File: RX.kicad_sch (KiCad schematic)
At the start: 1 part, among them U3 AD8285WBCPZ

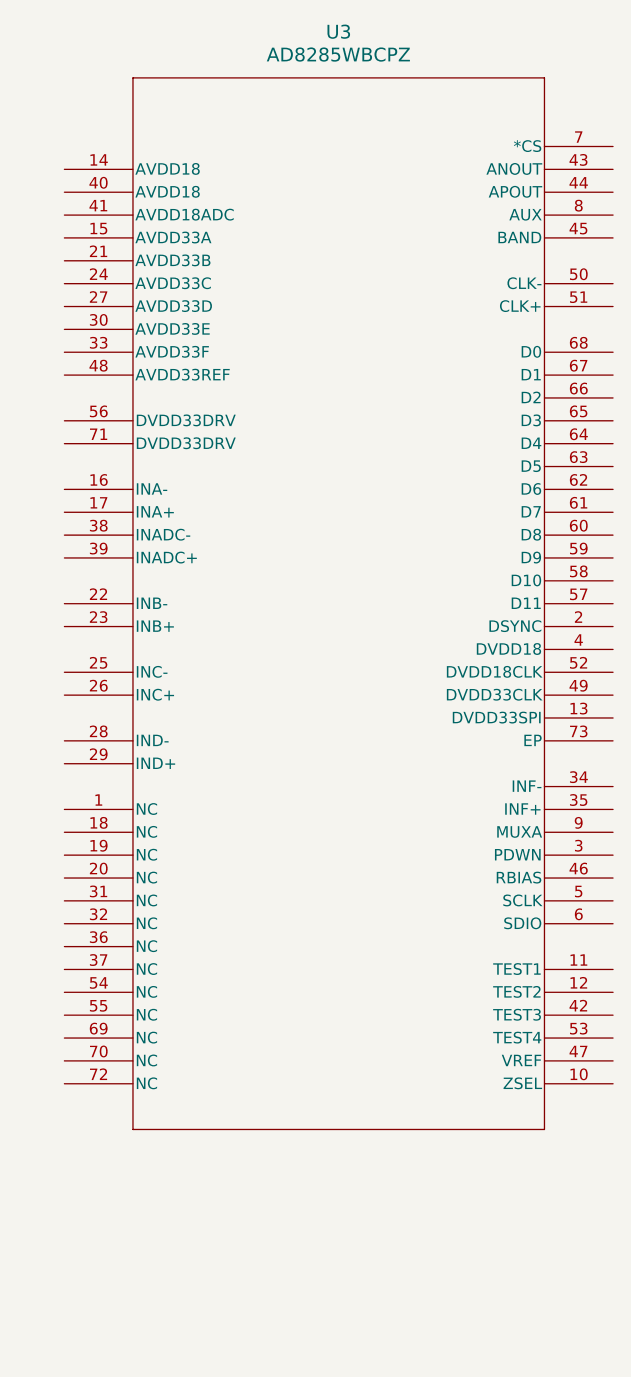
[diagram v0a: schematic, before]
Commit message: finished SOM 5V power, migrated altium stuff, finished pin study, added USB PHY (revise HS capability)
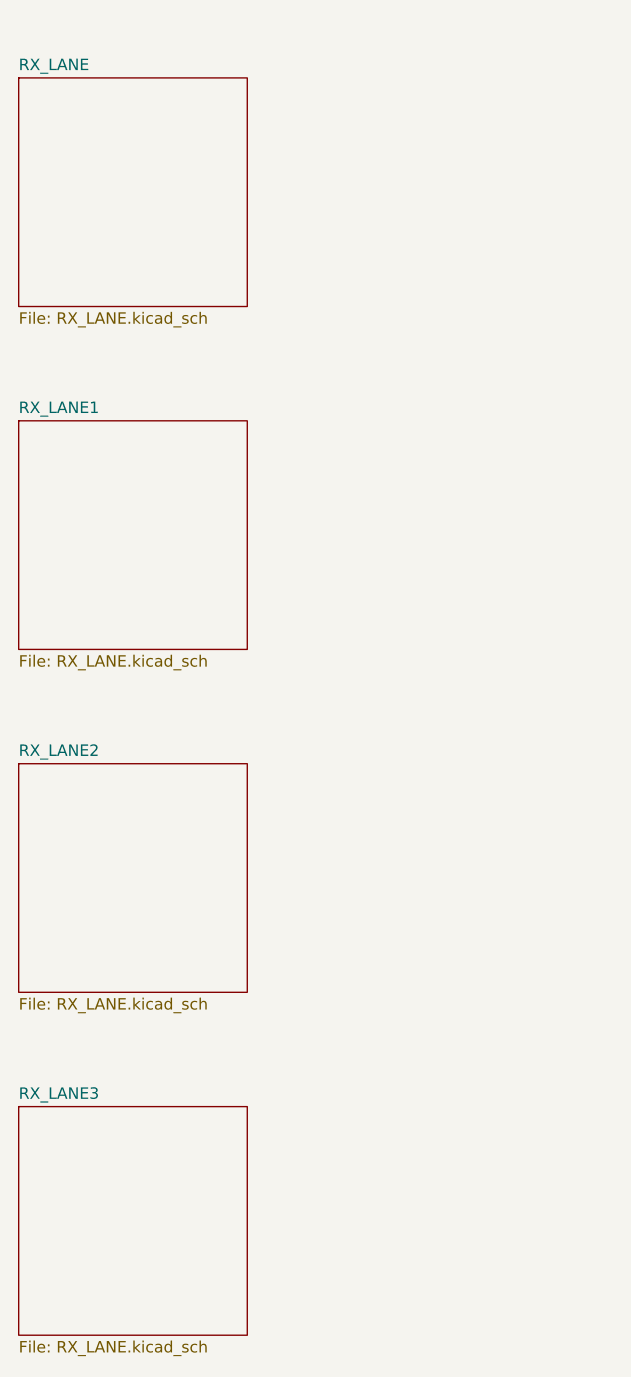
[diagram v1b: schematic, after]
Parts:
- removed U3: AD8285WBCPZ, CP_72_5_ADI, symbol AD8285WBCPZ:AD8285WBCPZ
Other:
- added sheet RX_LANE (RX_LANE.kicad_sch)
- added sheet RX_LANE1 (RX_LANE.kicad_sch)
- added sheet RX_LANE2 (RX_LANE.kicad_sch)
- added sheet RX_LANE3 (RX_LANE.kicad_sch)

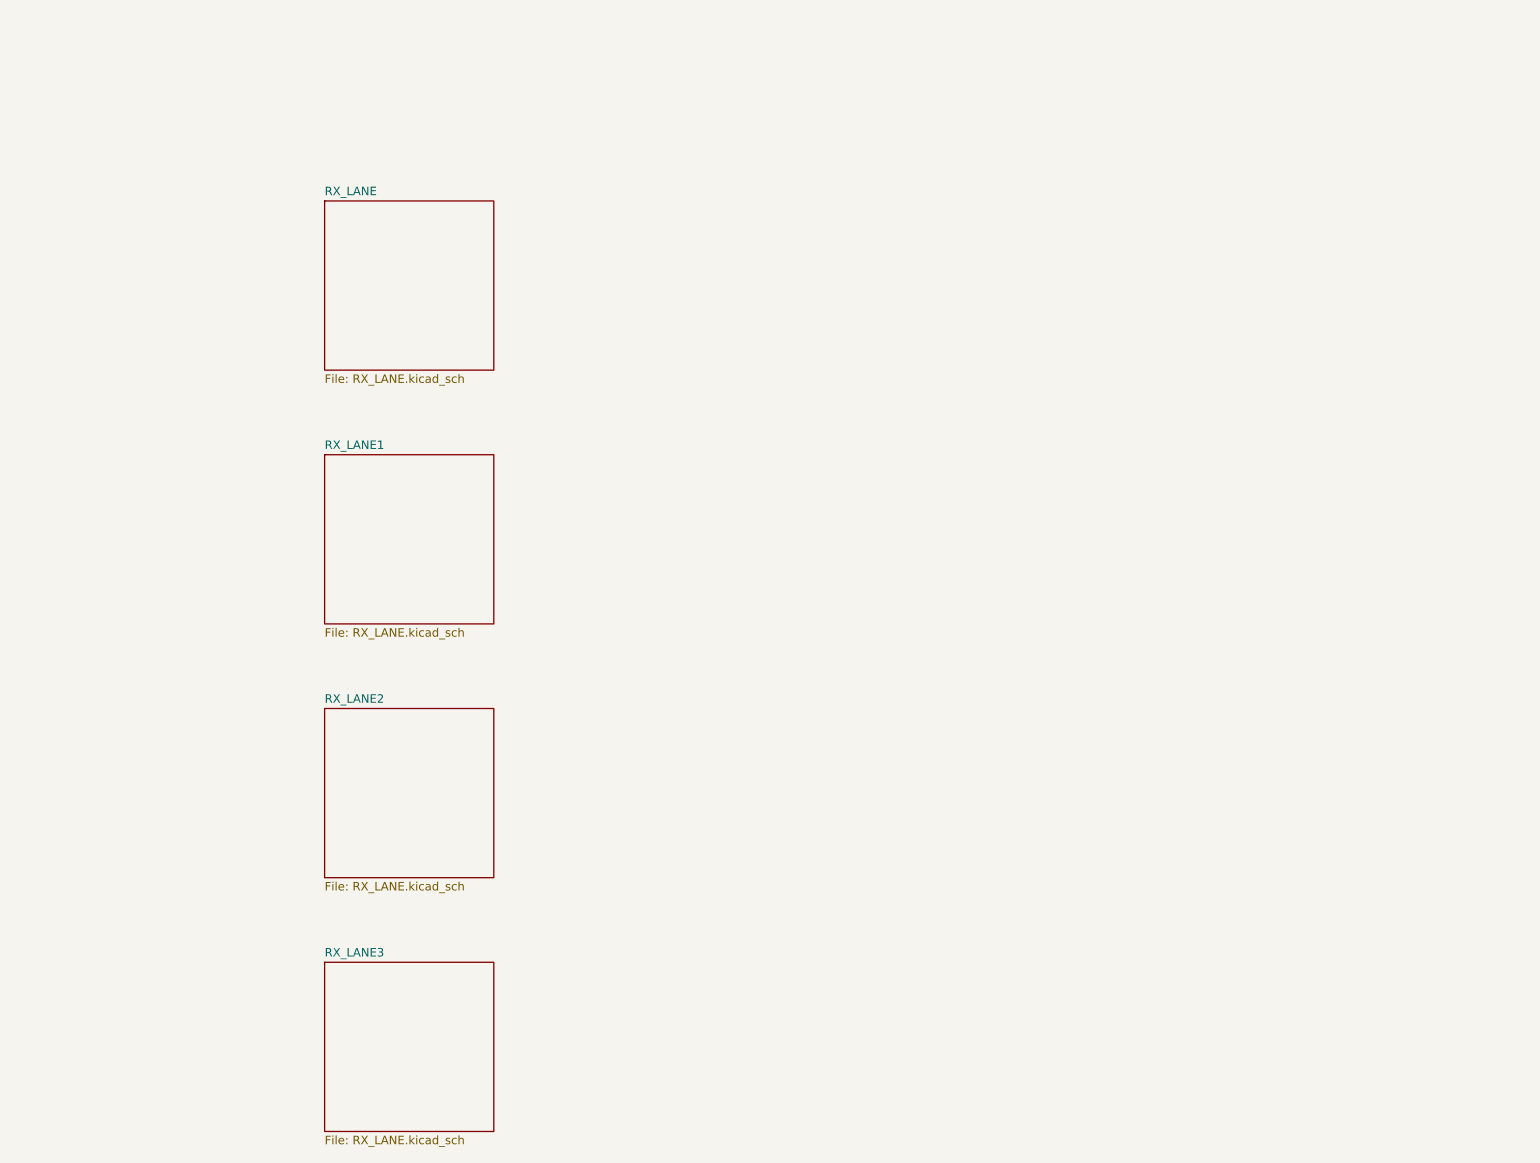
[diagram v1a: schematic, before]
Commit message: added ADC clock fanout, added 3A buck
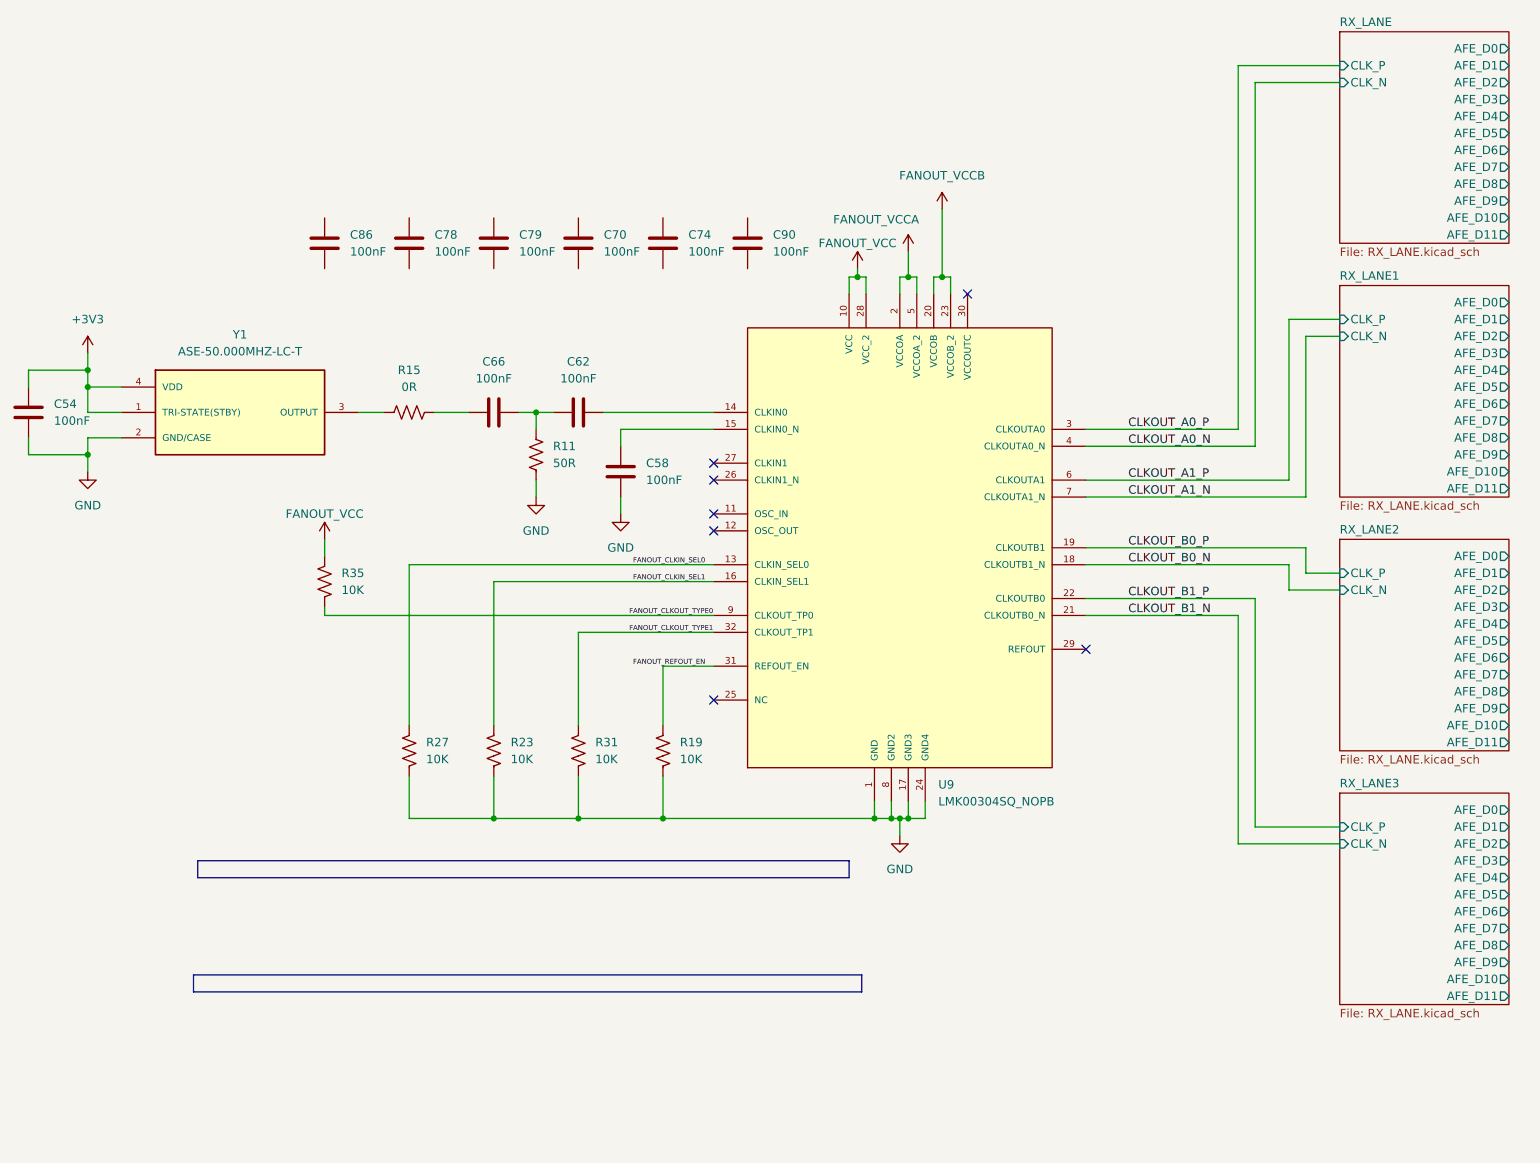
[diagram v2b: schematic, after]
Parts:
- added C54, C58, C62, C66, C70, C74, C78, C79, C86, C90: 100nF, symbol Device:C
- added R11: 50R, symbol Device:R_US
- added R15: 0R, symbol Device:R_US
- added R19, R23, R27, R31, R35: 10K, symbol Device:R_US
- added U9: LMK00304SQ_NOPB, LMK00304SQ_NOPB:WQFN-32, symbol LMK00304SQ_NOPB:LMK00304SQ_NOPB
- added Y1: ASE-50.000MHZ-LC-T, ASE-50.000MHZ-LC-T:XTAL_ASE-50.000MHZ-LC-T, symbol ASE-50.000MHZ-LC-T:ASE-50.000MHZ-LC-T
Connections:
- new net: R15.2, Y1.3 (OUTPUT)
- new net: C62.2, C66.1, R11.2
- new net: C66.2, R15.1
- new net: C62.1, U9.14 (CLKIN0)
- new net: C58.2, U9.15 (CLKIN0_N)
- new net +3V3: C54.2, Y1.1 (TRI-STATE(STBY)), Y1.4 (VDD)
- new net CLKOUT_A0_N: U9.4 (CLKOUTA0_N)
- new net CLKOUT_A0_P: U9.3 (CLKOUTA0)
- new net CLKOUT_A1_N: U9.7 (CLKOUTA1_N)
- new net CLKOUT_A1_P: U9.6 (CLKOUTA1)
- new net CLKOUT_B0_N: U9.18 (CLKOUTB1_N)
- new net CLKOUT_B0_P: U9.19 (CLKOUTB1)
- new net CLKOUT_B1_N: U9.21 (CLKOUTB0_N)
- new net CLKOUT_B1_P: U9.22 (CLKOUTB0)
- new net FANOUT_CLKIN_SEL0: R27.1, U9.13 (CLKIN_SEL0)
- new net FANOUT_CLKIN_SEL1: R23.1, U9.16 (CLKIN_SEL1)
- new net FANOUT_CLKOUT_TYPE0: R35.2, U9.9 (CLKOUT_TP0)
- new net FANOUT_CLKOUT_TYPE1: R31.1, U9.32 (CLKOUT_TP1)
- new net FANOUT_REFOUT_EN: R19.1, U9.31 (REFOUT_EN)
- new net FANOUT_VCC: R35.1, U9.10 (VCC), U9.28 (VCC_2)
- new net FANOUT_VCCA: U9.2 (VCCOA), U9.5 (VCCOA_2)
- new net FANOUT_VCCB: U9.20 (VCCOB), U9.23 (VCCOB_2)
- new net GND: C54.1, C58.1, R11.1, R19.2, R23.2, R27.2, R31.2, U9.1 (GND), U9.17 (GND3), U9.24 (GND4), U9.8 (GND2), Y1.2 (GND/CASE)
- no-connect marks 0 -> 7
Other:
- sheet RX_LANE ports: added AFE_D0, AFE_D1, AFE_D10, AFE_D11, AFE_D2, AFE_D3, AFE_D4, AFE_D5, AFE_D6, AFE_D7, AFE_D8, AFE_D9, CLK_N, CLK_P; removed none
- sheet RX_LANE1 ports: added AFE_D0, AFE_D1, AFE_D10, AFE_D11, AFE_D2, AFE_D3, AFE_D4, AFE_D5, AFE_D6, AFE_D7, AFE_D8, AFE_D9, CLK_N, CLK_P; removed none
- sheet RX_LANE2 ports: added AFE_D0, AFE_D1, AFE_D10, AFE_D11, AFE_D2, AFE_D3, AFE_D4, AFE_D5, AFE_D6, AFE_D7, AFE_D8, AFE_D9, CLK_N, CLK_P; removed none
- sheet RX_LANE3 ports: added AFE_D0, AFE_D1, AFE_D10, AFE_D11, AFE_D2, AFE_D3, AFE_D4, AFE_D5, AFE_D6, AFE_D7, AFE_D8, AFE_D9, CLK_N, CLK_P; removed none

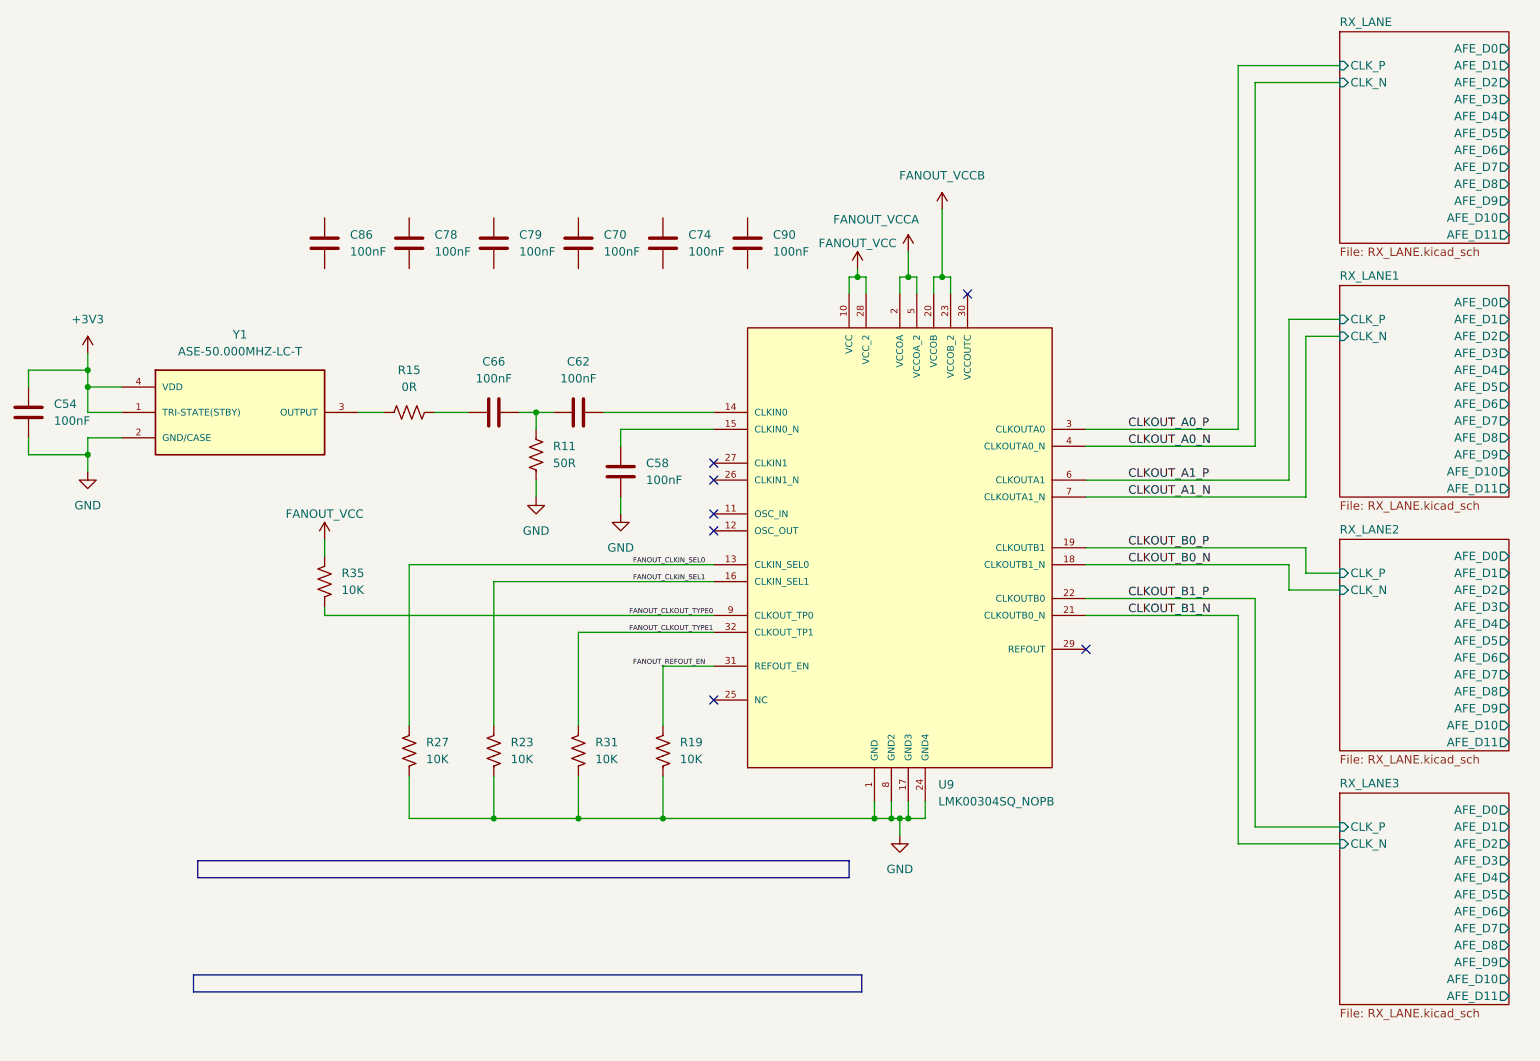
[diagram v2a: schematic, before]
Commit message: finished HV rails (revise, ai), added LDO instances, ready to bind & supply
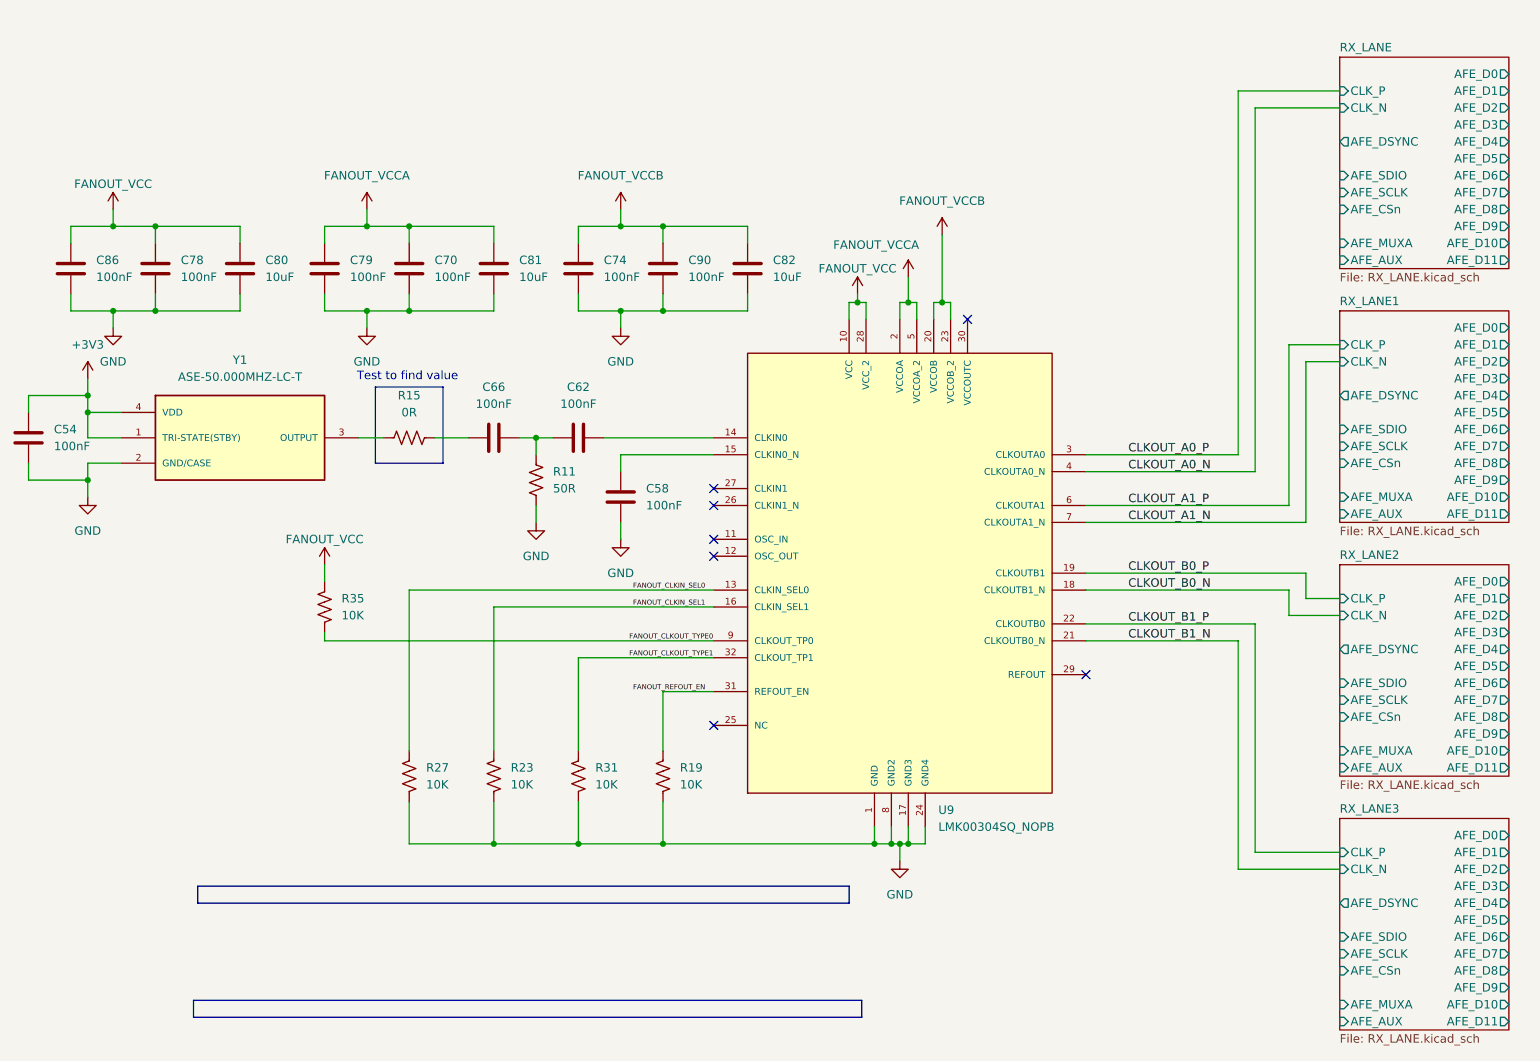
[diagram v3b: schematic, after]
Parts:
- added C80, C81, C82: 10uF, symbol Device:C
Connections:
- net FANOUT_VCC: now also C78.2, C86.2, C80.2
- net FANOUT_VCCA: now also C70.2, C79.2, C81.2
- net FANOUT_VCCB: now also C74.2, C90.2, C82.2
- net GND: now also C70.1, C74.1, C78.1, C79.1, C86.1, C90.1, C80.1, C81.1, C82.1
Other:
- sheet RX_LANE ports: added AFE_AUX, AFE_CSn, AFE_DSYNC, AFE_MUXA, AFE_SCLK, AFE_SDIO; removed none
- sheet RX_LANE1 ports: added AFE_AUX, AFE_CSn, AFE_DSYNC, AFE_MUXA, AFE_SCLK, AFE_SDIO; removed none
- sheet RX_LANE2 ports: added AFE_AUX, AFE_CSn, AFE_DSYNC, AFE_MUXA, AFE_SCLK, AFE_SDIO; removed none
- sheet RX_LANE3 ports: added AFE_AUX, AFE_CSn, AFE_DSYNC, AFE_MUXA, AFE_SCLK, AFE_SDIO; removed none
- note added: "Test to find value"
- moved on the sheet: C54, C58, C62, C66, C70, C74, C78, C79, C86, C90, R11, R15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
